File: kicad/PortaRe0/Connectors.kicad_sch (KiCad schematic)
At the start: 7 parts

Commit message: Docs: session21終了処理・PROGRESS/index更新・connectorsシート完成・ERC対処
- connectors シート完成（J_SBC_HDMI / J_FAN配置完了）
- hdmi_adapter シート新設（別基板 / J_MICROHDMI Conn_02x08 + C2856805）
- J_FAN: F16FB選定（16×16×4.5mm 5V）/ BSS138回路 / FAN_PWM GlobalLabel
- 全シートERC実施・対処完了（VL812未接続ピン / SWD NC / DC10FB追加等）

Co-Authored-By: Claude Sonnet 4.6 <noreply@anthropic.com>
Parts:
- added D9: 1N4148W, PortaRe0:SOD-123_L2.8-W1.8-LS3.7-RD, symbol PortaRe0:1N4148WT4
- added FPC2: J_SBC_HDMI, PortaRe0:FPC-SMD_24P-P0.50_FPC-05F-24PH20, symbol PortaRe0:FPC-05F-24PH20
- added J6: Fan, symbol Connector:Conn_01x02_Socket
- added Q1: BSS138, PortaRe0:SOT-23-3_L2.9-W1.6-P1.90-LS2.8-BR, symbol PortaRe0:BSS138_C52895
- added R56: 1kΩ, symbol Device:R_Small
- added R57: 10kΩ, symbol Device:R_Small
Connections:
- net 5V_SYS: now also D9.1 (K), FPC2.18, J6.1 (Pin_1)
- net GNDPWR: now also FPC2.11, FPC2.14, FPC2.17, FPC2.2, FPC2.20, FPC2.21, FPC2.22, FPC2.23, FPC2.24, FPC2.25, FPC2.26, FPC2.5, FPC2.8, Q1.2 (S), R57.1
- net HDMI_CLKN: now also FPC2.13
- net HDMI_CLKP: now also FPC2.12
- net HDMI_D0N: now also FPC2.10
- net HDMI_D0P: now also FPC2.9
- net HDMI_D1N: now also FPC2.7
- net HDMI_D1P: now also FPC2.6
- net HDMI_D2N: now also FPC2.4
- net HDMI_D2P: now also FPC2.3
- net HDMI_HPD: now also FPC2.1; no longer FPC1.19
- net HDMI_SCL: now also FPC2.15
- net HDMI_SDA: now also FPC2.16
- new net: D9.2 (A), J6.2 (Pin_2), Q1.3 (D)
- new net: Q1.1 (G), R56.1, R57.2
- new net FAN_PWM: R56.2
- new net HDMI_CEC: FPC1.19, FPC2.19

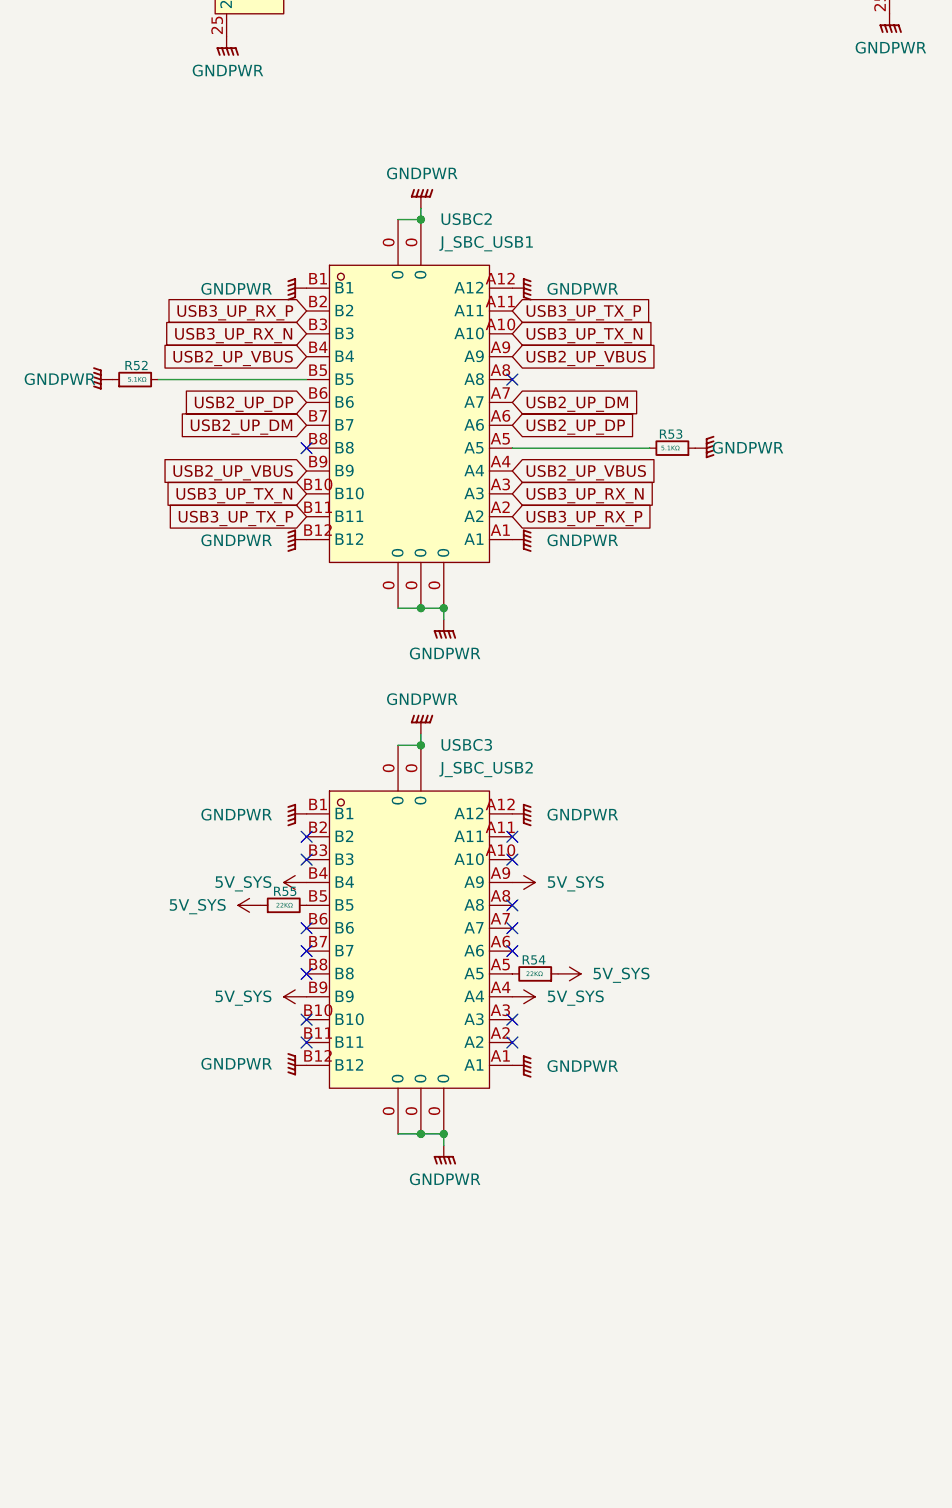
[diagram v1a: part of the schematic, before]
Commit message: KiCad: usb_adapterシート新設・connectorsシート整理
- usb_adapter.kicad_sch 新設（J_SBC_USB1/J_SBC_USB2を移動）
- FPCテール直挿し方式採用（中間コネクタなし）
- FPC 24pin ピン割り当て確定（差動ペア間GND配置）
- connectorsシートにC2856805（ZIF）×2追加
- .gitignore: kicad/PDF/ を除外に追加

Co-Authored-By: Claude Sonnet 4.6 <noreply@anthropic.com>
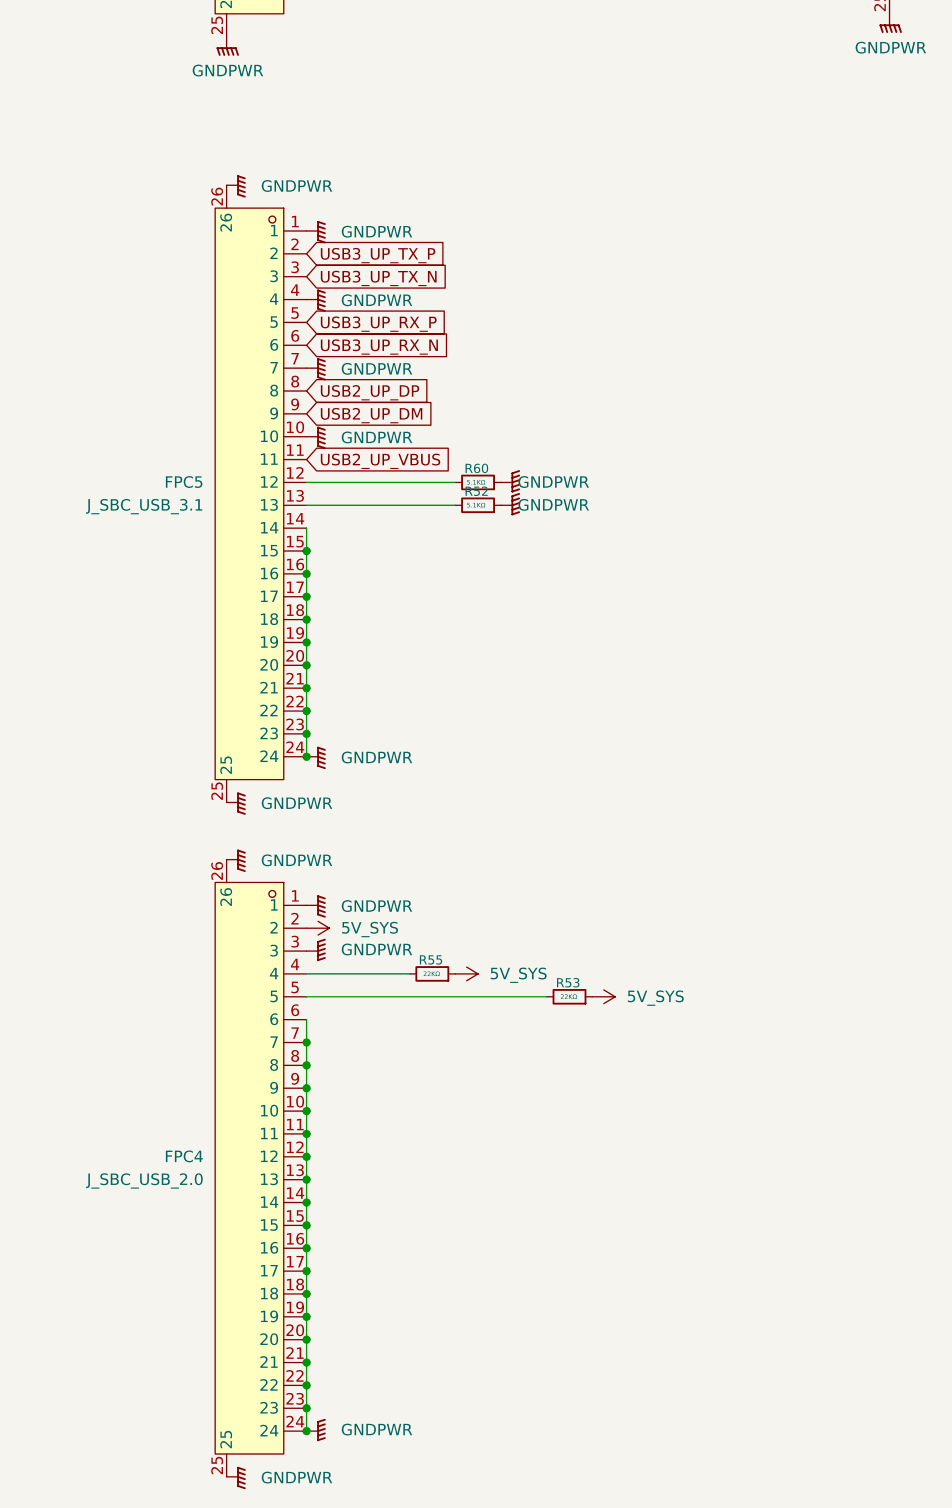
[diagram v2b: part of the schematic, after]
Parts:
- removed R54: 22KΩ, symbol Device:R_Small
- removed USBC2: J_SBC_USB1, PortaRe0:USB-C-SMD_TYPE-C-USB-3, symbol PortaRe0:TYPE-C3.1_C168690
- removed USBC3: J_SBC_USB2, PortaRe0:USB-C-SMD_TYPE-C-USB-3, symbol PortaRe0:TYPE-C3.1_C168690
- added FPC4: J_SBC_USB_2.0, PortaRe0:FPC-SMD_24P-P0.50_FPC-05F-24PH20, symbol PortaRe0:FPC-05F-24PH20
- added FPC5: J_SBC_USB_3.1, PortaRe0:FPC-SMD_24P-P0.50_FPC-05F-24PH20, symbol PortaRe0:FPC-05F-24PH20
- added R60: 5.1KΩ, symbol Device:R_Small
- R53: value 5.1KΩ -> 22KΩ
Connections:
- net 5V_SYS: now also R53.1, FPC4.2
- net GNDPWR: now also FPC4.1, FPC4.10, FPC4.11, FPC4.12, FPC4.13, FPC4.14, FPC4.15, FPC4.16, FPC4.17, FPC4.18, FPC4.19, FPC4.20, FPC4.21, FPC4.22, FPC4.23, FPC4.24, FPC4.25, FPC4.26, FPC4.3, FPC4.6, FPC4.7, FPC4.8, FPC4.9, FPC5.1, FPC5.10, FPC5.14, FPC5.15, FPC5.16, FPC5.17, FPC5.18, FPC5.19, FPC5.20, FPC5.21, FPC5.22, FPC5.23, FPC5.24, FPC5.25, FPC5.26, FPC5.4, FPC5.7, R60.1; no longer R53.1
- net USB2_UP_DM: now also FPC5.9
- net USB2_UP_DP: now also FPC5.8
- net USB2_UP_VBUS: now also FPC5.11
- net USB3_UP_RX_N: now also FPC5.6
- net USB3_UP_RX_P: now also FPC5.5
- net USB3_UP_TX_N: now also FPC5.3
- net USB3_UP_TX_P: now also FPC5.2
- net at R55.2: now also FPC4.4
- net at R53.2: now also FPC4.5
- net at R52.2: now also FPC5.13
- new net: FPC5.12, R60.2
- no-connect marks 16 -> 0
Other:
- moved on the sheet: R52, R55

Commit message: KiCad: 未コミットの回路図変更を追加
Co-Authored-By: Claude Sonnet 4.6 <noreply@anthropic.com>
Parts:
- R52, R60: value 5.1KΩ -> 5.1kΩ
- R53, R55: value 22KΩ -> 22kΩ
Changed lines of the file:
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@@
 			)
 		)
-		(property "Value" "22KΩ"
+		(property "Value" "22kΩ"
 			(at 86.614 195.58 90)
 			(effects
@@
 			)
 		)
-		(property "Value" "22KΩ"
+		(property "Value" "22kΩ"
 			(at 101.854 198.12 90)
 			(effects
@@
 			)
 		)
-		(property "Value" "5.1KΩ"
+		(property "Value" "5.1kΩ"
 			(at 91.44 143.51 90)
 			(effects
@@
 			)
 		)
-		(property "Value" "5.1KΩ"
+		(property "Value" "5.1kΩ"
 			(at 91.44 140.97 90)
 			(effects

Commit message: KiCad/Docs: session30終了処理・フットプリント割り当て完了・コネクタ確定
- フットプリント全割り当て完了（全シート）
- 新規フットプリント追加: SKSCLBE010/SKRPABE010/クリスタル/インダクタ×3/JST PHコネクタ×2
- コネクタ確定: バッテリー=B8B-PH-K-S(C157974) / SPK+FAN=B2B-PH-K-S(C131337)
- J5(hdmi_adapter): PinHeader_2x08_P2.00mm_Vertical
- Claude.md: ファン制御 RP2040 #1 GP26→BSS138→J6 に更新
- passive_parts.txt: コネクタセクション追加

Co-Authored-By: Claude Sonnet 4.6 <noreply@anthropic.com>
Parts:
- J6: footprint (none) -> PortaRe0:CONN-TH_B2B-PH-K-S
- R52, R53, R55, R56, R57, R60: footprint (none) -> Resistor_SMD:R_0603_1608Metric
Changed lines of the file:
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@@
 			)
 		)
-		(property "Footprint" ""
+		(property "Footprint" "Resistor_SMD:R_0603_1608Metric"
 			(at 87.63 195.58 0)
 			(effects
@@
 			)
 		)
-		(property "Footprint" ""
+		(property "Footprint" "Resistor_SMD:R_0603_1608Metric"
 			(at 187.96 137.16 0)
 			(effects
@@
 			)
 		)
-		(property "Footprint" ""
+		(property "Footprint" "PortaRe0:CONN-TH_B2B-PH-K-S"
 			(at 226.06 121.92 0)
 			(effects
@@
 			)
 		)
-		(property "Footprint" ""
+		(property "Footprint" "Resistor_SMD:R_0603_1608Metric"
 			(at 191.77 140.97 0)
 			(effects
@@
 			)
 		)
-		(property "Footprint" ""
+		(property "Footprint" "Resistor_SMD:R_0603_1608Metric"
 			(at 102.87 198.12 0)
 			(effects
@@
 			)
 		)
-		(property "Footprint" ""
+		(property "Footprint" "Resistor_SMD:R_0603_1608Metric"
 			(at 92.71 143.51 0)
 			(effects
@@
 			)
 		)
-		(property "Footprint" ""
+		(property "Footprint" "Resistor_SMD:R_0603_1608Metric"
 			(at 92.71 140.97 0)
 			(effects

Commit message: Docs/KiCad: session31終了処理・PROGRESS/index更新
- キルスイッチ確定: MSK12C02(C431540) EN制御方式・KiCad配線完了
- ヘッドフォンジャック確定: PJ-307C(C16684) TH / 配線・pull-up完了
- J4バッテリーコネクタ: S8B-PH-K-S-LF-SN(C157915) 水平型確定
- BOM Y4フットプリント修正
- 新規ライブラリ追加: MSK12C02/PJ-307C/S8B-PH-K-S他
- Phase 2 回路設計 全シート完了

Co-Authored-By: Claude Sonnet 4.6 <noreply@anthropic.com>
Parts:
- J6: footprint PortaRe0:CONN-TH_B2B-PH-K-S -> PortaRe0:CONN-TH_S2B-PH-K-S-LF-SN
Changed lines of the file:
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@@
 			)
 		)
-		(property "Footprint" "PortaRe0:CONN-TH_B2B-PH-K-S"
+		(property "Footprint" "PortaRe0:CONN-TH_S2B-PH-K-S-LF-SN"
 			(at 226.06 121.92 0)
 			(effects
